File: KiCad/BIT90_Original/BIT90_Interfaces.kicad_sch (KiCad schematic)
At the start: 7 parts, among them CN1a KO, CN1b KI, CN2 Cartridge, CN3 Expansion

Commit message: Added "Processor" Sheet 6-1
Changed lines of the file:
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@@
 	)
 	(global_label "~{WAIT}"
-		(shape input)
+		(shape bidirectional)
 		(at 85.09 135.89 270)
 		(fields_autoplaced yes)
@@
 		)
 		(property "Intersheetrefs" "${INTERSHEET_REFS}"
-			(at 85.09 142.9876 90)
+			(at 85.09 144.0989 90)
 			(effects
 				(font
@@
 	)
 	(global_label "~{DISM}"
-		(shape bidirectional)
+		(shape output)
 		(at 39.37 123.19 90)
 		(fields_autoplaced yes)
@@
 		)
 		(property "Intersheetrefs" "${INTERSHEET_REFS}"
-			(at 39.37 114.5578 90)
+			(at 39.37 115.6691 90)
 			(effects
 				(font
@@
 	)
 	(global_label "RES"
-		(shape input)
+		(shape output)
 		(at 49.53 135.89 270)
 		(fields_autoplaced yes)
@@
 	)
 	(global_label "~{INT}"
-		(shape input)
+		(shape bidirectional)
 		(at 87.63 135.89 270)
 		(fields_autoplaced yes)
@@
 		)
 		(property "Intersheetrefs" "${INTERSHEET_REFS}"
-			(at 87.63 141.7781 90)
+			(at 87.63 142.8894 90)
 			(effects
 				(font
@@
 	)
 	(global_label "~{RST}"
-		(shape bidirectional)
+		(shape input)
 		(at 80.01 123.19 90)
 		(fields_autoplaced yes)
@@
 		)
 		(property "Intersheetrefs" "${INTERSHEET_REFS}"
-			(at 80.01 115.6464 90)
+			(at 80.01 116.7577 90)
 			(effects
 				(font
@@
 	)
 	(global_label "INT"
-		(shape bidirectional)
+		(shape output)
 		(at 87.63 123.19 90)
 		(fields_autoplaced yes)
@@
 		)
 		(property "Intersheetrefs" "${INTERSHEET_REFS}"
-			(at 87.63 116.1906 90)
-			(effects
-				(font
+			(at 87.63 117.3019 90)
+			(effects
+				(font

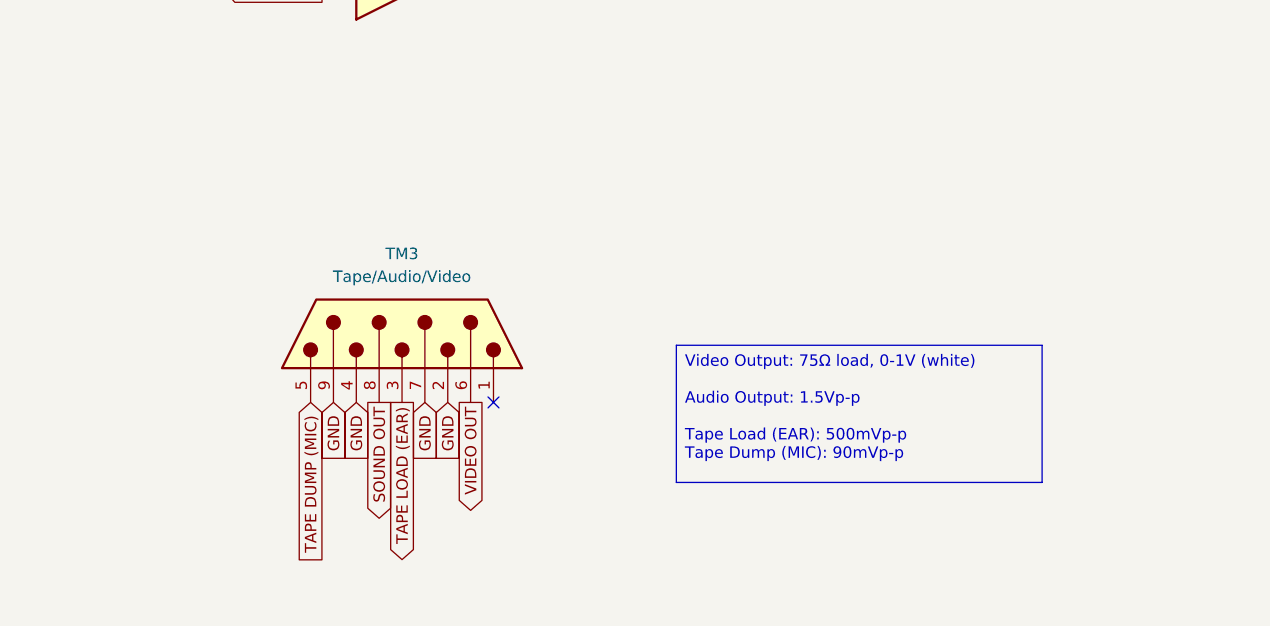
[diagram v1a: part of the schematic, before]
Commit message: Completed keyboard schematic
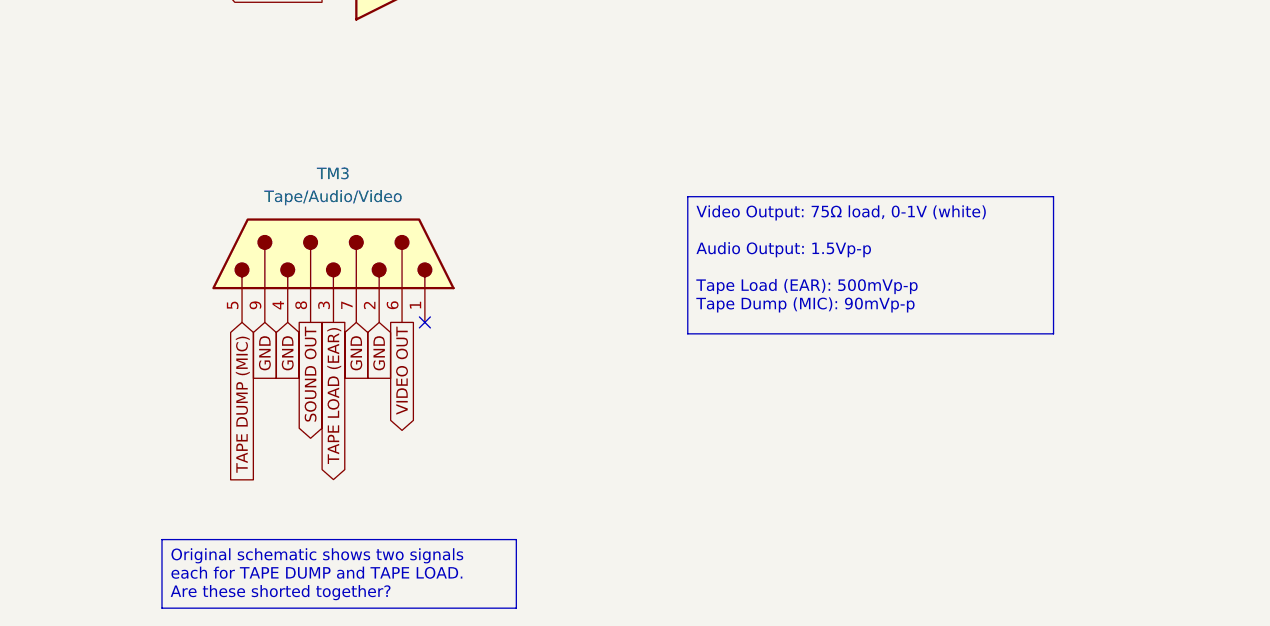
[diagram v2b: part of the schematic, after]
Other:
- moved on the sheet: TM3
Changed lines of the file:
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@@
+		)
+	)
+	(text_box "Original schematic shows two signals each for TAPE DUMP and TAPE LOAD.\nAre these shorted together?"
+		(exclude_from_sim no)
+		(at 153.67 151.13 0)
+		(size 39.37 7.62)
+		(margins 0.9525 0.9525 0.9525 0.9525)
+		(stroke
+			(width 0)
+			(type solid)
+		)
+		(fill
+			(type none)
+		)
+		(effects
+			(font
+				(size 1.27 1.27)
+			)
+			(justify left top)
 		)
 	)
 	(text_box "Video Output: 75Ω load, 0-1V (white)\n\nAudio Output: 1.5Vp-p\n\nTape Load (EAR): 500mVp-p\nTape Dump (MIC): 90mVp-p"
 		(exclude_from_sim no)
-		(at 210.82 129.54 0)
+		(at 212.09 113.03 0)
 		(size 40.64 15.24)
 		(margins 0.9525 0.9525 0.9525 0.9525)
@@
 	)
 	(no_connect
-		(at 190.5 135.89)
+		(at 182.88 127)
 	)
 	(no_connect
@@
 	(global_label "GND"
 		(shape input)
-		(at 172.72 135.89 270)
-		(fields_autoplaced yes)
-		(effects
-			(font
-				(size 1.27 1.27)
-			)
-			(justify right)
-		)
-		(property "Intersheetrefs" "${INTERSHEET_REFS}"
-			(at 172.72 142.7457 90)
+		(at 165.1 127 270)
+		(fields_autoplaced yes)
+		(effects
+			(font
+				(size 1.27 1.27)
+			)
+			(justify right)
+		)
+		(property "Intersheetrefs" "${INTERSHEET_REFS}"
+			(at 165.1 133.8557 90)
 			(effects
 				(font
@@
 	(global_label "GND"
 		(shape input)
-		(at 182.88 135.89 270)
-		(fields_autoplaced yes)
-		(effects
-			(font
-				(size 1.27 1.27)
-			)
-			(justify right)
-		)
-		(property "Intersheetrefs" "${INTERSHEET_REFS}"
-			(at 182.88 142.7457 90)
+		(at 175.26 127 270)
+		(fields_autoplaced yes)
+		(effects
+			(font
+				(size 1.27 1.27)
+			)
+			(justify right)
+		)
+		(property "Intersheetrefs" "${INTERSHEET_REFS}"
+			(at 175.26 133.8557 90)
 			(effects
 				(font
@@
 	(global_label "SOUND OUT"
 		(shape output)
-		(at 177.8 135.89 270)
-		(fields_autoplaced yes)
-		(effects
-			(font
-				(size 1.27 1.27)
-			)
-			(justify right)
-		)
-		(property "Intersheetrefs" "${INTERSHEET_REFS}"
-			(at 177.8 149.9424 90)
+		(at 170.18 127 270)
+		(fields_autoplaced yes)
+		(effects
+			(font
+				(size 1.27 1.27)
+			)
+			(justify right)
+		)
+		(property "Intersheetrefs" "${INTERSHEET_REFS}"
+			(at 170.18 141.0524 90)
 			(effects
 				(font
@@
 	(global_label "VIDEO OUT"
 		(shape output)
-		(at 187.96 135.89 270)
-		(fields_autoplaced yes)
-		(effects
-			(font
-				(size 1.27 1.27)
-			)
-			(justify right)
-		)
-		(property "Intersheetrefs" "${INTERSHEET_REFS}"
-			(at 187.96 148.9143 90)
+		(at 180.34 127 270)
+		(fields_autoplaced yes)
+		(effects
+			(font
+				(size 1.27 1.27)
+			)
+			(justify right)
+		)
+		(property "Intersheetrefs" "${INTERSHEET_REFS}"
+			(at 180.34 140.0243 90)
 			(effects
 				(font
@@
 	(global_label "GND"
 		(shape input)
-		(at 185.42 135.89 270)
-		(fields_autoplaced yes)
-		(effects
-			(font
-				(size 1.27 1.27)
-			)
-			(justify right)
-		)
-		(property "Intersheetrefs" "${INTERSHEET_REFS}"
-			(at 185.42 142.7457 90)
+		(at 177.8 127 270)
+		(fields_autoplaced yes)
+		(effects
+			(font
+				(size 1.27 1.27)
+			)
+			(justify right)
+		)
+		(property "Intersheetrefs" "${INTERSHEET_REFS}"
+			(at 177.8 133.8557 90)
 			(effects
 				(font
@@
 	(global_label "TAPE LOAD (EAR)"
 		(shape output)
-		(at 180.34 135.89 270)
-		(fields_autoplaced yes)
-		(effects
-			(font
-				(size 1.27 1.27)
-			)
-			(justify right)
-		)
-		(property "Intersheetrefs" "${INTERSHEET_REFS}"
-			(at 180.34 155.2038 90)
+		(at 172.72 127 270)
+		(fields_autoplaced yes)
+		(effects
+			(font
+				(size 1.27 1.27)
+			)
+			(justify right)
+		)
+		(property "Intersheetrefs" "${INTERSHEET_REFS}"
+			(at 172.72 146.3138 90)
 			(effects
 				(font
@@
 	(global_label "GND"
 		(shape input)
-		(at 175.26 135.89 270)
-		(fields_autoplaced yes)
-		(effects
-			(font
-				(size 1.27 1.27)
-			)
-			(justify right)
-		)
-		(property "Intersheetrefs" "${INTERSHEET_REFS}"
-			(at 175.26 142.7457 90)
+		(at 167.64 127 270)
+		(fields_autoplaced yes)
+		(effects
+			(font
+				(size 1.27 1.27)
+			)
+			(justify right)
+		)
+		(property "Intersheetrefs" "${INTERSHEET_REFS}"
+			(at 167.64 133.8557 90)
 			(effects
 				(font
@@
 	(global_label "TAPE DUMP (MIC)"
 		(shape input)
-		(at 170.18 135.89 270)
-		(fields_autoplaced yes)
-		(effects
-			(font
-				(size 1.27 1.27)
-			)
-			(justify right)
-		)
-		(property "Intersheetrefs" "${INTERSHEET_REFS}"
-			(at 170.18 155.6271 90)
+		(at 162.56 127 270)
+		(fields_autoplaced yes)
+		(effects
+			(font
+				(size 1.27 1.27)
+			)
+			(justify right)
+		)
+		(property "Intersheetrefs" "${INTERSHEET_REFS}"
+			(at 162.56 146.7371 90)
 			(effects
 				(font
@@
 	(symbol
 		(lib_id "Connector:DE9_Pins")
-		(at 180.34 128.27 90)
+		(at 172.72 119.38 90)
 		(unit 1)
 		(exclude_from_sim no)
@@
 		(fields_autoplaced yes)
 		(property "Reference" "TM3"
-			(at 180.34 119.38 90)
+			(at 172.72 110.49 90)
 			(effects
 				(font
@@
 		)
 		(property "Value" "Tape/Audio/Video"
-			(at 180.34 121.92 90)
+			(at 172.72 113.03 90)
 			(effects
 				(font
@@
 		)
 		(property "Footprint" ""
-			(at 180.34 128.27 0)
+			(at 172.72 119.38 0)
 			(effects
 				(font
@@
 		)
 		(property "Datasheet" "~"
-			(at 180.34 128.27 0)
+			(at 172.72 119.38 0)
 			(effects
 				(font
@@
 		)
 		(property "Description" "9-pin D-SUB connector, pins (male)"
-			(at 180.34 128.27 0)
-			(effects
-				(font
+			(at 172.72 119.38 0)
+			(effects
+				(font

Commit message: Added "Joystick, Audio, Tape Out" schematic
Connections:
- net SOUND OUT is gone; now on net AUDIO OUT: TM3.8
- net CAR1 renamed ~{CAR1}
- net CAR2 renamed ~{CAR2}
- net CAR3 renamed ~{CAR3}
- net CAR4 renamed ~{CAR4}
- net CPU0 renamed CPUΦ
- net EXT0 renamed EXTΦ
- net R0 renamed RΦ
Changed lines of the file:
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@@
-		)
-	)
-	(text_box "Original schematic shows two signals each for TAPE DUMP and TAPE LOAD.\nAre these shorted together?"
-		(exclude_from_sim no)
-		(at 153.67 151.13 0)
-		(size 39.37 7.62)
-		(margins 0.9525 0.9525 0.9525 0.9525)
-		(stroke
-			(width 0)
-			(type solid)
-		)
-		(fill
-			(type none)
-		)
-		(effects
-			(font
-				(size 1.27 1.27)
-			)
-			(justify left top)
 		)
 	)
@@
 		)
 	)
-	(global_label "CAR2"
+	(global_label "~{CAR2}"
 		(shape input)
 		(at 66.04 71.12 90)
@@
 		)
 	)
-	(global_label "R0"
+	(global_label "RΦ"
 		(shape input)
 		(at 59.69 135.89 270)
@@
 		)
 		(property "Intersheetrefs" "${INTERSHEET_REFS}"
-			(at 59.69 141.3547 90)
+			(at 59.69 141.4757 90)
 			(effects
 				(font
@@
 		)
 	)
-	(global_label "SOUND OUT"
-		(shape output)
+	(global_label "AUDIO OUT"
+		(shape input)
 		(at 170.18 127 270)
 		(fields_autoplaced yes)
@@
 		)
 		(property "Intersheetrefs" "${INTERSHEET_REFS}"
-			(at 170.18 141.0524 90)
+			(at 170.18 140.2058 90)
 			(effects
 				(font
@@
 	)
 	(global_label "VIDEO OUT"
-		(shape output)
+		(shape input)
 		(at 180.34 127 270)
 		(fields_autoplaced yes)
@@
 		)
 	)
-	(global_label "EXT0"
+	(global_label "EXTΦ"
 		(shape input)
 		(at 46.99 135.89 270)
@@
 		)
 		(property "Intersheetrefs" "${INTERSHEET_REFS}"
-			(at 46.99 143.4108 90)
+			(at 46.99 143.5318 90)
 			(effects
 				(font
@@
 		)
 	)
-	(global_label "CPU0"
+	(global_label "CPUΦ"
 		(shape input)
 		(at 72.39 135.89 270)
@@
 		)
 		(property "Intersheetrefs" "${INTERSHEET_REFS}"
-			(at 72.39 143.9552 90)
+			(at 72.39 144.0762 90)
 			(effects
 				(font
@@
 		)
 	)
-	(global_label "CAR4"
+	(global_label "~{CAR4}"
 		(shape input)
 		(at 58.42 83.82 270)
@@
 		)
 	)
-	(global_label "CAR3"
+	(global_label "~{CAR3}"
 		(shape input)
 		(at 91.44 71.12 90)
@@
 		)
 	)
-	(global_label "CAR1"
+	(global_label "~{CAR1}"
 		(shape input)
 		(at 71.12 71.12 90)

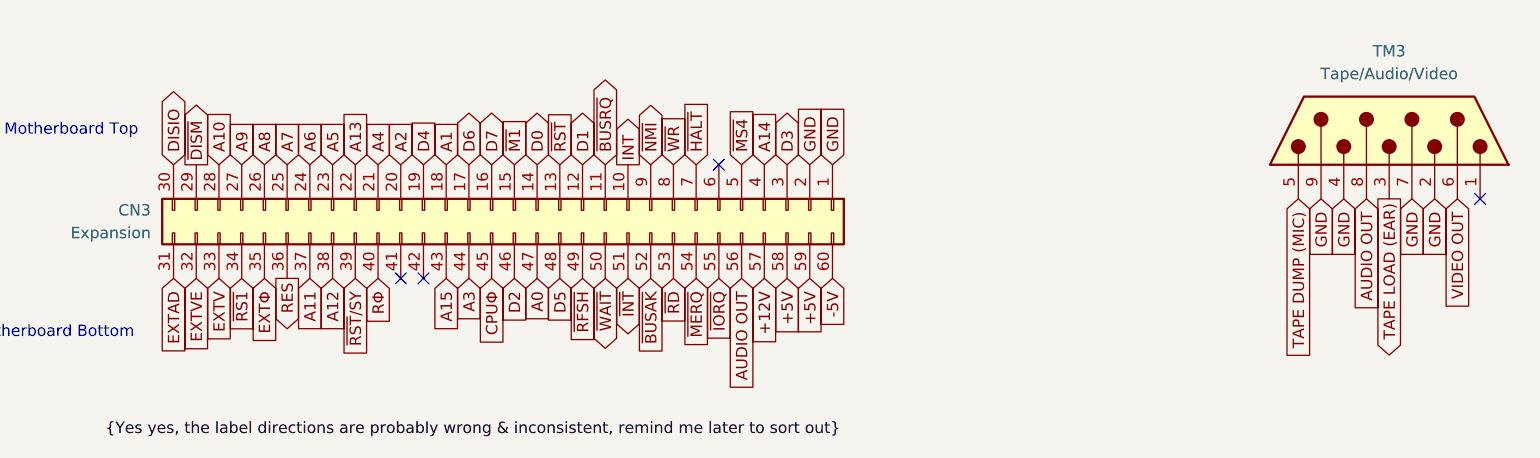
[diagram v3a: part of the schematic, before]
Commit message: Minor schematic corrections
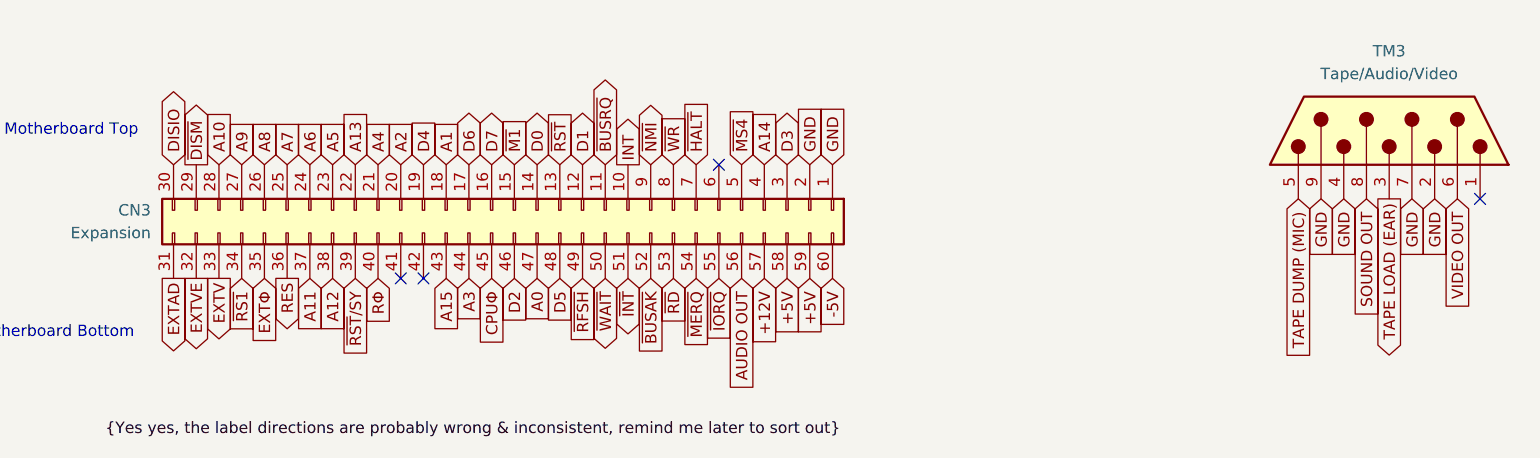
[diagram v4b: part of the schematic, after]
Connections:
- net AUDIO OUT: no longer TM3.8
- new net SOUND OUT: TM3.8
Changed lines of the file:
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@@
 		(rev "WIP")
 		(company "Brett Hallen")
-		(comment 4 "Based on original schematics from BIT Corporation")
+		(comment 4 "Based on original schematics from BIT Corporation (普澤有限公司)")
 	)
 	(text "Motherboard Bottom"
@@
 	)
 	(global_label "EXTAD"
-		(shape input)
+		(shape output)
 		(at 36.83 135.89 270)
 		(fields_autoplaced yes)
@@
 	)
 	(global_label "EXTVE"
-		(shape input)
+		(shape output)
 		(at 39.37 135.89 270)
 		(fields_autoplaced yes)
@@
 		)
 	)
-	(global_label "AUDIO OUT"
+	(global_label "SOUND OUT"
 		(shape input)
 		(at 170.18 127 270)
@@
 		)
 		(property "Intersheetrefs" "${INTERSHEET_REFS}"
-			(at 170.18 140.2058 90)
+			(at 170.18 141.0524 90)
 			(effects
 				(font
@@
 	)
 	(global_label "EXTV"
-		(shape input)
+		(shape output)
 		(at 41.91 135.89 270)
 		(fields_autoplaced yes)

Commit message: Completed original schematic redraw
Well, didn't finish the Video Encoder (PAL) sheet as I'm not going to use any of it in the new design.
Moved the audio output from that sheet to the Joystick/Audio/Tape out sheet where the sound generator is.
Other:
- moved on the sheet: CN1a, CN1b, CN2, CN3, TM1, TM2, TM3
